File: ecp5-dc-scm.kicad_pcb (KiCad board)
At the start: 6 copper layers, 90 x 120.4 mm, 366 parts, among them IC1 TPS54561, J1 WE-RJ45_7499111121A, J10 61300611121, J11 DC_SOCKET, J12 S2B-PH-K-S_LF__SN_, J2 1-2199230-6, J3 543630489, J4 M20-7830642, J5 SFF-TA-1002-4C+, J6 2X05, J7 61301021121, J8 61301021121, J9 61301221121, Q1 2N7002, Q10 IRLML6402TRPBF, Q11 IRLML6402TRPBF, Q12 IRLML6402TRPBF, Q2 2N7002, Q3 2N7002, Q4 2N7002, Q5 2N7002, Q6 2N7002, Q7 2N7002, Q8 IRLML6402TRPBF, Q9 IRLML6402TRPBF, U1 KSZ9031RNXCA, U10 TPS62823DLCT, U11 TPS62823DLCT, U12 TPS62823DLCT, U13 TPS62823DLCT, U14 ECP5UM5G_85_CABGA756, U15 TPS62823DLCT, U16 LM21212-2, U17 SN74LVC1G11DBVR, U2 W25Q32JVSSIQ_TR, U3 W25Q32JVSSIQ_TR, U4 W25Q32JVSSIQ_TR, U5 W25Q32JVSSIQ_TR, U6 NVT2008DQ,115, U7 AS4C256M16D3, U8 TPS51200DRC, U9 LM3881MME_NOPB, Y1 ABM8G-25.000MHZ-18-D2Y-T

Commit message: Add ethernet and power supply component placement
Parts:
- removed C100, C101, C115, C116, C117, C118, C152, C157, C165, C171, C176, C181, C48, C92: C_4u7_0402, antmicro-footprints:0402-cap
- removed C102, C104, C106, C108, C110, C131, C134, C64, C99: C_10n_0402, antmicro-footprints:0402-cap
- removed C103, C105, C119, C120, C121, C122, C123, C124, C125, C126, C127, C129, C130, C132, C133, C135, C136, C138, C139, C140, C141, C142, C143, C144, C145, C146, C147, C148, C149, C150, C151, C153, C154, C155, C156, C158, C159, C160, C161, C162, C163, C164, C166, C167, C168, C169, C170, C172, C173, C174, C175, C177, C178, C179, C180, C182, C183, C184, C185, C35, C36, C37, C38, C49, C50, C51, C52, C53, C54, C55, C56, C58, C59, C60, C61, C93, C94, C95: C_470n_0402, antmicro-footprints:0402-cap
- removed C107, C109, C111, C137: C_1n_0402, antmicro-footprints:0402-res
- removed C112, C113, C114, C196, C91, C97, C98: C_47u_0603, antmicro-footprints:0603-cap
- removed C128, C188, C27, C28, C29, C30, C39, C57, C62, C63, C96: C_100n_0402, antmicro-footprints:0402-cap
- removed C186, C187, C189, C192, C194, C31, C32, C33, C34, C75, C76, C77, C78, C83, C84, C85, C86, C87, C88, C89, C90: C_10u_0402, antmicro-footprints:0402-cap
- removed C190, C79, C80, C81, C82: C_120p_0402, antmicro-footprints:0402-res
- removed C191: C_1n8_0402, antmicro-footprints:0402-cap
- removed C193: C_180p_0402, antmicro-footprints:0402-cap
- removed C195: C_750p_0402, antmicro-footprints:0402-res
- removed D1: KP-1608CGCK, antmicro-footprints:LED_0603
- removed D3, D4, D5, D6, D7, D8, D9: LG_L29K-G2J1-24-Z, antmicro-footprints:LED_0603
- removed F1: 0466003.NR, antmicro-footprints:1206-Fuse-Littelfuse-0466-0-0-MFG
- removed FB4, FB5, FB6, FB7, FB8: BLM18PG121SN1D, antmicro-footprints:0603-res
- removed J12: S2B-PH-K-S_LF__SN_, antmicro-footprints:PinHeader_1x2_P2mm_Drill1mm_RA
- removed J4: M20-7830642, antmicro-footprints:PinHeader_6x2_P2.54mm_Vertical
- removed L2, L3, L4, L5: IHLP1212AEERR47M11, antmicro-footprints:IHLP-1212AE
- removed L6: 470n/IHLP1212, Inductor_SMD:L_Vishay_IHLP-1212
- removed L7: XAL5030-801, antmicro-footprints:Coilcraft-XAL5030
- removed Q1, Q2, Q3, Q4, Q5, Q6, Q7: 2N7002, antmicro-footprints:SOT-23-3
- removed Q10, Q11, Q12, Q8, Q9: IRLML6402TRPBF, antmicro-footprints:SOT-23-3
- removed R100, R101, R102, R15, R16, R25, R26, R27, R28, R63, R64, R65, R96, R97, R98, R99: R_1k_0402, antmicro-footprints:0402-res
- removed R17, R19, R20, R29, R30, R31, R32, R33, R34, R35, R36, R37, R38, R39, R40, R41, R42, R43, R44, R86, R88, R89, R90, R91, R92, R93, R94, R95: R_10k_0402, antmicro-footprints:0402-res
- removed R18: R_330R_0402, antmicro-footprints:0402-res
- removed R21, R22, R23, R24, R85: R_4k7_0402, antmicro-footprints:0402-res
- removed R45, R46, R47, R48, R49, R50, R51, R52: R_357k_0402, antmicro-footprints:0402-res
- removed R53, R75: R_200k_0402, antmicro-footprints:0402-res
- removed R54, R55, R56: 8x51R_0602_array, antmicro-footprints:R_Array_Convex_8x0602
- removed R60: R_240R_0402, antmicro-footprints:0402-res
- removed R61, R62: R_51R_0402, antmicro-footprints:0402-res
- removed R73, R83: R_453k_0402, antmicro-footprints:0402-res
- removed R74, R76, R78, R80, R84: R_100k_0402, antmicro-footprints:0402-res
- removed R77, R79: R_124k_0402, antmicro-footprints:0402-res
- removed R81: R_10R_0603, antmicro-footprints:0603-res
- removed R82: R_47k_0402, antmicro-footprints:0402-res
- removed R87: R_470k_0402, antmicro-footprints:0402-res
- removed TP2: TP_SMD1MM, antmicro-footprints:Testpoint_smd_1mm
- removed U10, U11, U12, U13, U15: TPS62823DLCT, antmicro-footprints:QFN-8_2x1mm
- removed U16: LM21212-2, antmicro-footprints:HTSSOP-20_TI-PWP
- removed U17: SN74LVC1G11DBVR, antmicro-footprints:SOT-23-6
- removed U2, U3, U4, U5: W25Q32JVSSIQ_TR, antmicro-footprints:SOIC-8_W5.6mm
- removed U9: LM3881MME_NOPB, antmicro-footprints:VSSOP8-Texas_Instruments-DGK0008A
- added C65: C_2u2_0603_25V, antmicro-footprints:0603-cap, F.Cu at (73.4, 81.0)
- added C66: C_2u2_0603_25V, antmicro-footprints:0603-cap, F.Cu at (73.4, 79.6)
- added C67: C_2u2_0603_25V, antmicro-footprints:0603-cap, F.Cu at (73.4, 78.2)
- C1, C10, C11, C12, C13, C14, C15, C16, C17, C18, C19, C2, C21, C22, C23, C24, C25, C3, C4, C5, C6, C7, C8, C9, FB1, FB2, FB3: moved to B.Cu
- moved R11 199.6 mm to (111.9, 91.7), turned to 180 degrees
- moved C12 195.4 mm to (114.7, 91.2)
- moved C11 193.8 mm to (111.9, 92.2), turned to 180 degrees
- moved R5 193.0 mm to (119.4, 99.6), turned to 270 degrees
- moved C3 190.9 mm to (115.6, 99.5), turned to 270 degrees
- moved R2 190.6 mm to (117.4, 99.6), turned to 270 degrees
- moved R4 190.1 mm to (115.2, 99.6), turned to 270 degrees
- moved C8 190.0 mm to (120.9, 94.8), turned to 180 degrees
- moved C6 190.0 mm to (119.6, 96.6), turned to 90 degrees
- moved R12 189.7 mm to (111.9, 92.8), turned to 180 degrees
- moved FB2 188.7 mm to (117.9, 87.3), turned to 90 degrees
- moved C10 187.0 mm to (115.0, 87.6), turned to 90 degrees
- moved R8 186.8 mm to (121.5, 99.6), turned to 270 degrees
- moved C7 186.4 mm to (115.6, 96.6), turned to 90 degrees
- moved C15 185.9 mm to (117.6, 96.6), turned to 90 degrees
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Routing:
- net VCC1V2: track 0.00 -> 12.0 mm, vias 0 -> 5
- net Net-(C20-Pad1): track 0.00 -> 11.4 mm
- net Net-(C71-Pad1): track 0.00 -> 10.3 mm, vias 0 -> 2
- net GND: track 0.00 -> 10.0 mm
- net (no net): track 0.00 -> 9.13 mm
- net VCC3V3: track 0.00 -> 8.31 mm, vias 0 -> 3
- net Net-(C26-Pad1): track 0.00 -> 8.02 mm
- net /DDR3/DDR3_VTT: track 0.00 -> 6.03 mm
- net /Ethernet/AVDDL: track 0.00 -> 5.91 mm, vias 0 -> 2
- net Net-(R70-Pad2): track 0.00 -> 5.24 mm, vias 0 -> 2
- net Net-(C10-Pad1): track 0.00 -> 4.97 mm, vias 0 -> 2
- net RGMII_RXD3: track 0.00 -> 4.22 mm, vias 0 -> 1
- net Net-(F2-Pad1): track 0.00 -> 4.09 mm
- net RGMII_RXD1: track 0.00 -> 3.90 mm, vias 0 -> 1
- net RGMII_RX_CLK: track 0.00 -> 3.84 mm, vias 0 -> 1
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- added copper zone on F.Cu, net GND
- added copper zone on F.Cu, net Net-(C71-Pad1)
- added copper zone on F.Cu, net Net-(C72-Pad1)
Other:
- board text added: "5V0 supply"
- board text added: "DDR3 PMIC"
- board text removed: "TPM"

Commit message: Fix outline
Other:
- outline, holes or cut-outs redrawn

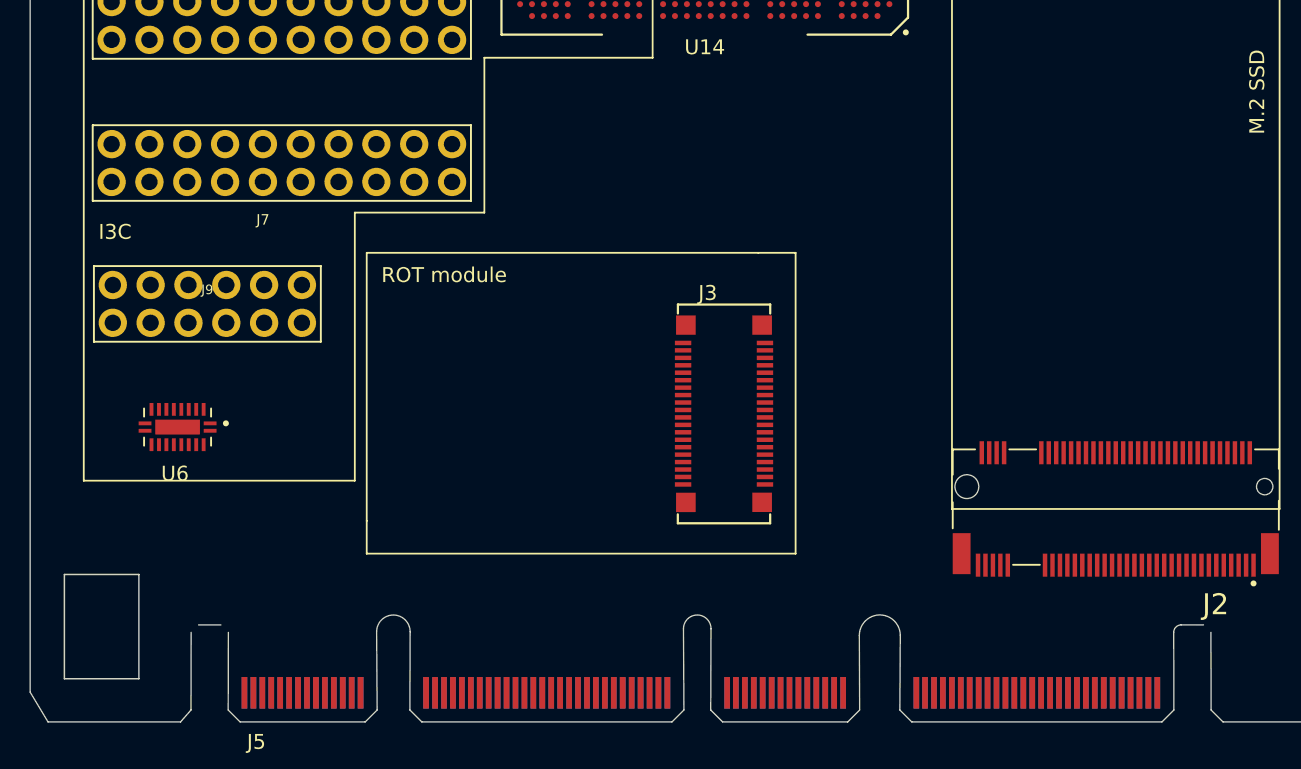
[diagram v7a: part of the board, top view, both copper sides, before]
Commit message: Close PCB outline
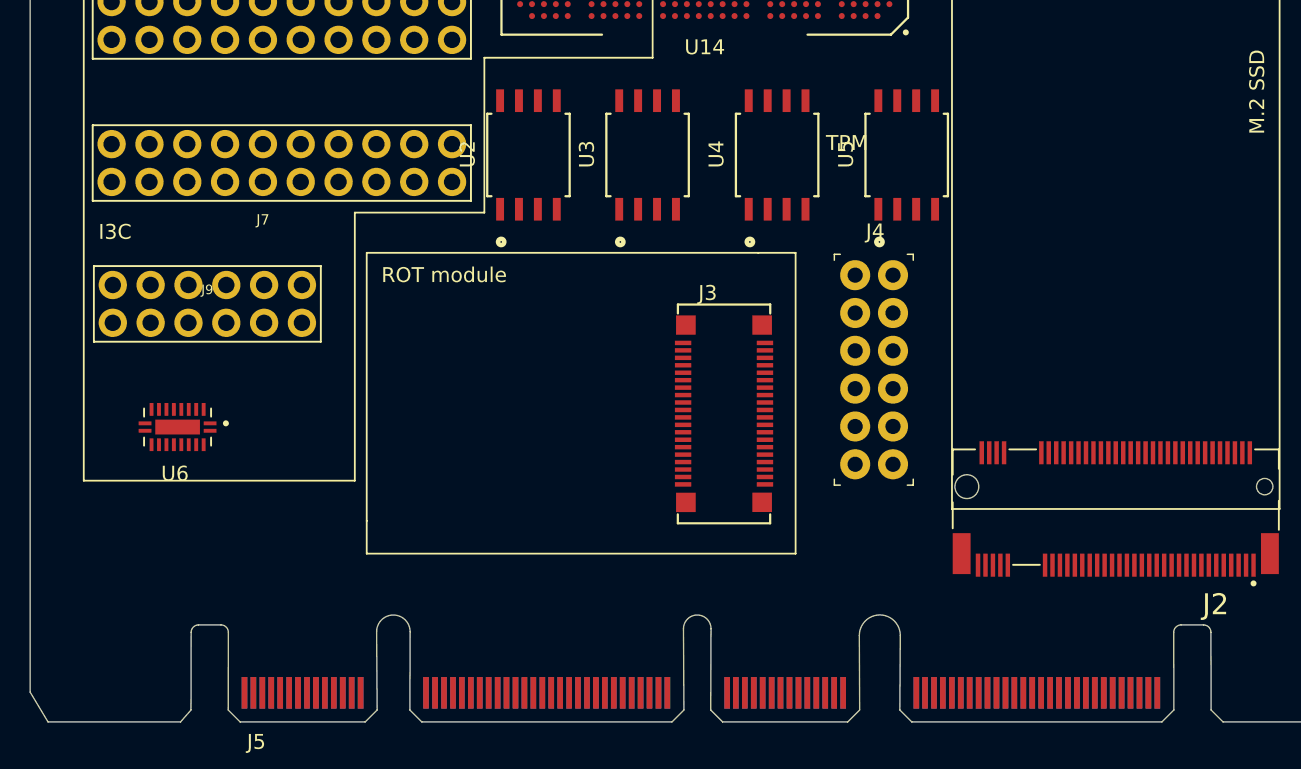
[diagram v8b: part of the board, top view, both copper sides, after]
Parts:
- added J4: M20-7830642, antmicro-footprints:PinHeader_6x2_P2.54mm_Vertical, F.Cu at (115.5, 149.3)
- added U2: W25Q32JVSSIQ_TR, antmicro-footprints:W25Q32JVSSIQ, F.Cu at (93.6, 141.2)
- added U3: W25Q32JVSSIQ_TR, antmicro-footprints:W25Q32JVSSIQ, F.Cu at (101.6, 141.2)
- added U4: W25Q32JVSSIQ_TR, antmicro-footprints:W25Q32JVSSIQ, F.Cu at (110.3, 141.2)
- added U5: W25Q32JVSSIQ_TR, antmicro-footprints:W25Q32JVSSIQ, F.Cu at (119.0, 141.2)
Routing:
- net (no net): track 9.13 -> 10.0 mm
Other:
- outline, holes or cut-outs redrawn
- board text added: "TPM"
